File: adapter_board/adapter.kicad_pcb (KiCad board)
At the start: 2 copper layers, 100 x 80 mm, 25 parts, among them P101 CONN_01X12, P103 CONN_01X12, P104 CONN_01X02, P105 CONN_01X02, P106 CONN_01X02, P107 CONN_01X02, P108 CONN_01X01, P109 CONN_01X06, P110 CONN_01X06, P111 CONN_01X06, Q201 BC850, Q202 IRF530N, Q301 BC850, Q302 IRF530N, Q401 BC850, Q402 IRF530N

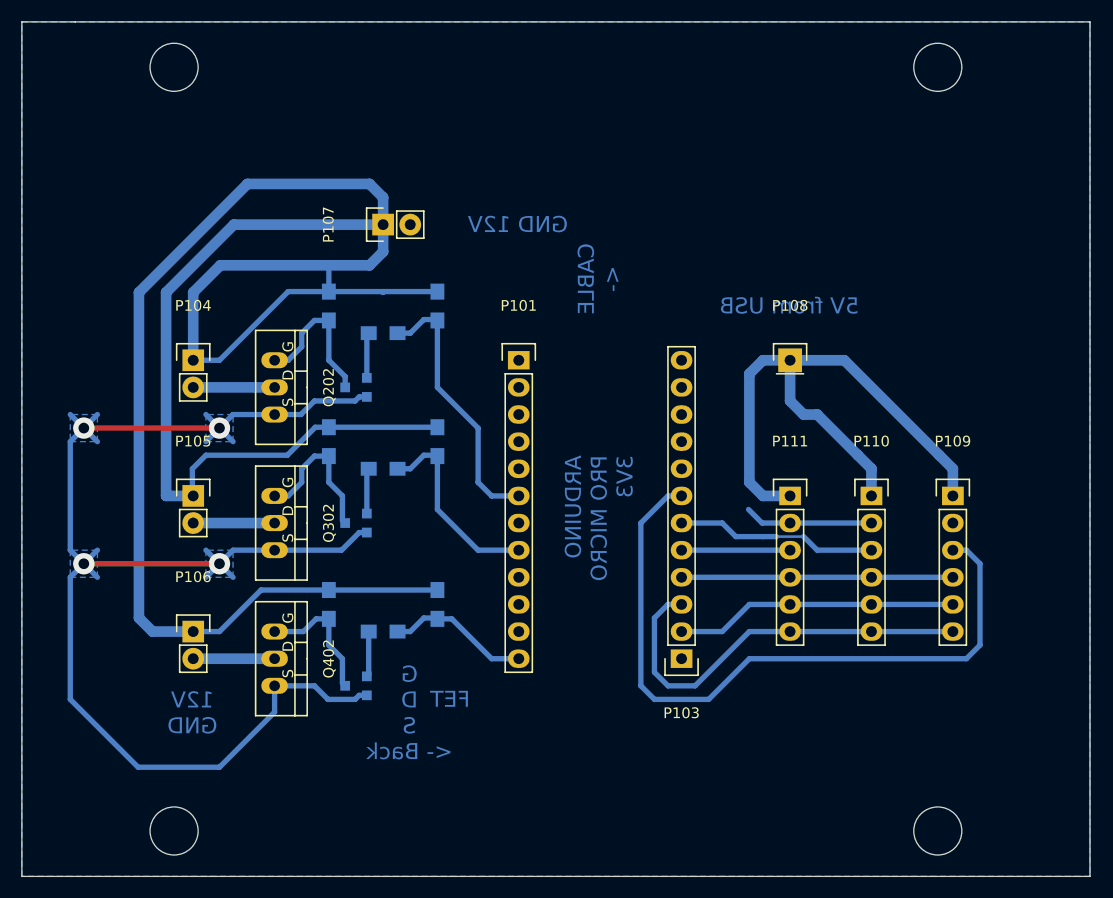
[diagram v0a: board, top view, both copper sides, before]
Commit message: enlargen pads for handsoldering
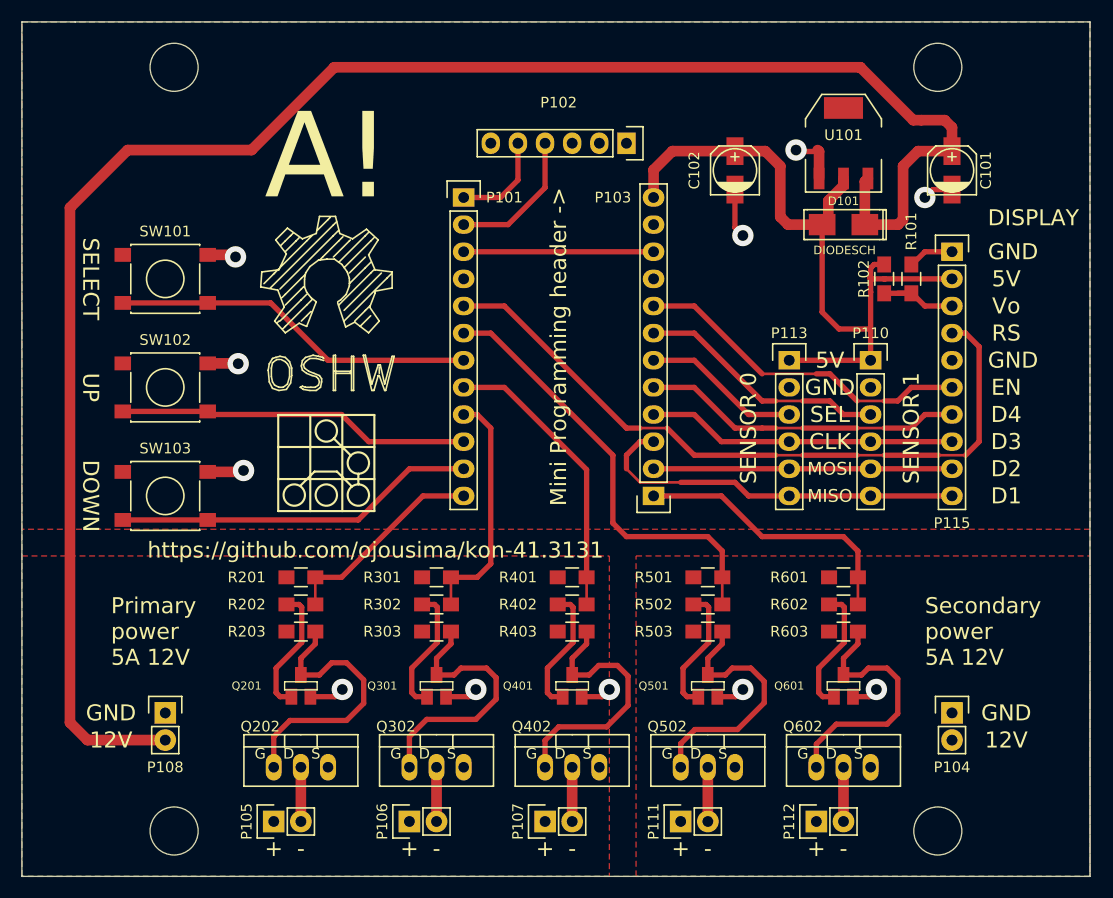
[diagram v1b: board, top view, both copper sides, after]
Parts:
- removed P109: CONN_01X06, Pin_Headers:Pin_Header_Straight_1x06
- added C101: 10u, SMD_Capacitors:c_elec_4x5.3, F.Cu at (132.1, 88.9)
- added C102: 100u, SMD_Capacitors:c_elec_4x5.3, F.Cu at (111.8, 88.9)
- added D101: DIODESCH, smd_diodes:SMA_WAVE, F.Cu at (121.9, 94.0)
- added LOGO101: OPEN_HARDWARE_2, Symbols:Symbol_OSHW-Logo_SilkScreen_BIG, F.Cu at (73.7, 80.0)
- added P102: CONN_01X06, Pin_Headers:Pin_Header_Straight_1x06, F.Cu at (101.6, 86.4)
- added P112: CONN_01X02, Pin_Headers:Pin_Header_Straight_1x02, F.Cu at (119.4, 149.9)
- added P113: CONN_01X06, Pin_Headers:Pin_Header_Straight_1x06, F.Cu at (116.8, 106.7)
- added P115: CONN_01X10, Pin_Headers:Pin_Header_Straight_1x10, F.Cu at (132.1, 96.5)
- added Q501: BC850, smd_packages_fork:SOT23EBC, F.Cu at (109.2, 137.2)
- added Q502: IRF530N, Transistors_TO-220:TO-220_FET-GDS_Vertical, F.Cu at (109.2, 144.8)
- added Q601: BC850, smd_packages_fork:SOT23EBC, F.Cu at (121.9, 137.2)
- added Q602: IRF530N, Transistors_TO-220:TO-220_FET-GDS_Vertical, F.Cu at (121.9, 144.8)
- added R101: R, Resistors_SMD:R_0805_HandSoldering, F.Cu at (125.7, 99.1)
- added R102: R, Resistors_SMD:R_0805_HandSoldering, F.Cu at (128.3, 99.1)
- added R501: 10k, Resistors_SMD:R_0805_HandSoldering, F.Cu at (109.2, 127.0)
- added R502: 1k, Resistors_SMD:R_0805_HandSoldering, F.Cu at (109.2, 129.5)
- added R503: 10k, Resistors_SMD:R_0805_HandSoldering, F.Cu at (109.2, 132.1)
- added R601: 10k, Resistors_SMD:R_0805_HandSoldering, F.Cu at (121.9, 127.0)
- added R602: 1k, Resistors_SMD:R_0805_HandSoldering, F.Cu at (121.9, 129.5)
- added R603: 10k, Resistors_SMD:R_0805_HandSoldering, F.Cu at (121.9, 132.1)
- added SW101: SPST, SMD_Switches:SW_SPST_PTS645, F.Cu at (58.4, 99.1)
- added SW102: SPST, SMD_Switches:SW_SPST_PTS645, F.Cu at (58.4, 109.2)
- added SW103: SPST, SMD_Switches:SW_SPST_PTS645, F.Cu at (58.4, 119.4)
- added U101: LD1117S50TR, SMD_Packages:SOT-223, F.Cu at (121.9, 86.4)
- P108: value CONN_01X01 -> CONN_01X02; footprint Pin_Headers:Pin_Header_Straight_1x01 -> Pin_Headers:Pin_Header_Straight_1x02
- P111: value CONN_01X06 -> CONN_01X02; footprint Pin_Headers:Pin_Header_Straight_1x06 -> Pin_Headers:Pin_Header_Straight_1x02
- Q201, Q301, Q401, R201, R202, R203, R301, R302, R303, R401, R402, R403: moved to F.Cu
- moved P104 78.3 mm to (132.1, 139.7)
- moved P108 67.2 mm to (58.4, 139.7)
- moved P107 57.9 mm to (94.0, 149.9)
- moved Q202 35.6 mm to (71.1, 144.8), turned to 0 degrees
- moved P111 32.2 mm to (106.7, 149.9), turned to 90 degrees
- moved P105 31.4 mm to (68.6, 149.9), turned to 90 degrees
- moved R203 30.6 mm to (71.1, 132.1), turned to 0 degrees
- moved Q402 29.7 mm to (96.5, 144.8), turned to 0 degrees
- moved R201 28.4 mm to (71.1, 127.0), turned to 0 degrees
- moved Q201 28.4 mm to (71.1, 137.2), turned to 180 degrees
- moved Q302 27.4 mm to (83.8, 144.8), turned to 0 degrees
- moved P106 26.9 mm to (81.3, 149.9), turned to 90 degrees
- moved R202 26.5 mm to (71.1, 129.5)
- moved R403 22.9 mm to (96.5, 132.1), turned to 0 degrees
- moved R303 20.4 mm to (83.8, 132.1), turned to 0 degrees
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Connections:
- net Net-(P103-Pad9) renamed /3V3
- P101 pad 10: Net-(P101-Pad10) -> /BT1
- P101 pad 11: Net-(P101-Pad11) -> /BT2
- P101 pad 12: /PWM2/INV_PWM -> /PWM0/INV_PWM
- P101 pad 3: Net-(P101-Pad3) -> /RESET
- P101 pad 4: /PWM0/GND -> GND
- P101 pad 5: /D2 -> /RS
- P101 pad 6: /PWM0/INV_PWM -> /PWM3/INV_PWM
- P101 pad 7: Net-(P101-Pad7) -> /BT0
- P101 pad 8: /PWM1/INV_PWM -> /PWM2/INV_PWM
- P101 pad 9: /D6 -> /PWM1/INV_PWM
- P103 pad 1: Net-(P103-Pad1) -> /PWM4/INV_PWM
- P103 pad 10: Net-(P103-Pad10) -> /RESET
- P103 pad 11: /PWM0/GND -> GND
- P103 pad 12: Net-(P103-Pad12) -> /5V
- P103 pad 5: /SEL0 -> /D4
- P103 pad 6: /SEL1 -> /SEL0
- P103 pad 7: /SEL2 -> /SEL1
- P103 pad 8: Net-(P103-Pad8) -> /SEL2
- P104 pad 1: /PWM0/12V -> GND
- P104 pad 2: /PWM0/Drain -> /PWM3/12V
- P105 pad 2: /PWM1/Drain -> /PWM0/Drain
- P106 pad 2: /PWM2/Drain -> /PWM1/Drain
- P107 pad 2: /PWM0/GND -> /PWM2/Drain
- P108 pad 1: /5V -> GND
- P110 pad 2: /PWM0/GND -> GND
- P111 pad 1: /5V -> /PWM3/12V
- P111 pad 2: /PWM0/GND -> /PWM3/Drain
- Q201 pad 1: /PWM0/GND -> GND
- Q202 pad S: /PWM0/GND -> GND
- Q301 pad 1: /PWM0/GND -> GND
- Q302 pad S: /PWM0/GND -> GND
- Q401 pad 1: /PWM0/GND -> GND
- Q402 pad S: /PWM0/GND -> GND
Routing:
- net /PWM0/GND: track 149.9 -> 0.00 mm, vias 4 -> 0
- net /RS: track 0.00 -> 66.5 mm
- net /PWM0/12V: track 218.8 -> 168.8 mm
- net /PWM3/INV_PWM: track 0.00 -> 41.4 mm
- net GND: track 0.00 -> 39.9 mm, vias 0 -> 11
- net /BT0: track 0.00 -> 34.1 mm
- net /BT2: track 0.00 -> 33.9 mm
- net /BT1: track 0.00 -> 33.5 mm
- net /SEL2: track 65.2 -> 32.1 mm
- net /D4: track 0.00 -> 30.0 mm
- net /PWM4/INV_PWM: track 0.00 -> 26.3 mm
- net Net-(Q601-Pad3): track 0.00 -> 24.6 mm
- net Net-(Q501-Pad3): track 0.00 -> 24.3 mm
- net /RESET: track 0.00 -> 17.8 mm
- net /PWM2/INV_PWM: track 13.5 -> 27.3 mm
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- added copper zone on F.Cu, net /PWM0/12V
- added copper zone on F.Cu, net /PWM3/12V
- added copper zone on B.Cu, net GND
- added copper zone on F.Cu, net GND
- removed copper zone on B.Cu, net /PWM0/GND
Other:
- net class Default: clearance 0.4 -> 0.25
- net class Power: clearance 0.4 -> 0.25
- net class thight removed
- rule trace_clearance: 0.4 -> 0.25
- board text added: "+"
- board text added: "-"
- board text added: "12V"
- board text added: "5V"
- board text added: "A!"
- board text added: "CLK"
- board text added: "D1"
- board text added: "D2"
- board text added: "D3"
- board text added: "D4"
- board text added: "DISPLAY"
- board text added: "DOWN"
- board text added: "EN"
- board text added: "GND"
- board text added: "MISO"
- board text added: "MOSI"
- board text added: "Mini Programming header ->"
- board text added: "Primary power 5A 12V"
- board text added: "RS"
- board text added: "SEL"
- board text added: "SELECT"
- board text added: "SENSOR 0"
- board text added: "SENSOR 1"
- board text added: "Secondary power 5A 12V"
- board text added: "UP"
- board text added: "Vo"
- board text added: "https://github.com/ojousima/kon-41.3131"
- board text removed: "12V GND"
- board text removed: "5V from USB"
- board text removed: "ARDUINO PRO MICRO 3V3"
- board text removed: "CABLE <-"
- board text removed: "FET"
- board text removed: "G D S <- Back"
- board text removed: "GND 12V"

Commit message: Final version
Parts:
- C102: footprint SMD_Capacitors:c_elec_4x5.3 -> SMD_Capacitors:c_elec_5x5.8
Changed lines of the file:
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@@
-(kicad_pcb (version 4) (host pcbnew "(2014-08-05 BZR 5054)-product")
+(kicad_pcb (version 4) (host pcbnew "(2015-02-06 BZR 5410)-product")
   (general
     (links 108)
     (no_connects 0)
-    (area 44.949999 74.949999 145.050001 155.050001)
+    (area 40.564287 74.899999 148.685715 165.200001)
     (thickness 1.6)
     (drawings 76)
@@
   (layers
     (0 F.Cu signal)
-    (31 B.Cu signal)
+    (31 B.Cu signal hide)
     (32 B.Adhes user)
     (33 F.Adhes user)
@@
     (visible_elements 7FFEFFFF)
     (pcbplotparams
-      (layerselection 0x00030_80000001)
-      (usegerberextensions false)
+      (layerselection 0x00008_00000000)
+      (usegerberextensions true)
       (excludeedgelayer true)
       (linewidth 0.100000)
@@
       (plotinvisibletext false)
       (padsonsilk false)
-      (subtractmaskfromsilk false)
+      (subtractmaskfromsilk true)
       (outputformat 1)
       (mirror false)
-      (drillshape 1)
+      (drillshape 0)
       (scaleselection 1)
-      (outputdirectory ""))
+      (outputdirectory gerber/))
   )
   (net 0 "")
@@
     (pad 1 smd rect (at 1.80086 0 90) (size 2.60096 1.6002) (layers F.Cu F.Paste F.Mask)
       (net 12 /PWM0/12V))
-    (pad 2 smd rect (at -1.80086 0 90) (size 2.60096 1.6002) (layers F.Cu F.Paste F.Mask)
-      (net 40 GND))
-    (model Capacitors_SMD.3dshapes/c_elec_4x5.3.wrl
-      (at (xyz 0 0 0))
-      (scale (xyz 1 1 1))
-      (rotate (xyz 0 0 0))
-    )
-  )
-  (module SMD_Capacitors:c_elec_4x5.3 (layer F.Cu)
-    (at 111.76 88.9 90)
-    (descr "SMT capacitor, aluminium electrolytic, 4x5.3")
-    (fp_text reference C102 (at 0 -3.81 90) (layer F.SilkS)
-      (effects (font (size 1 1) (thickness 0.15)))
-    )
-    (fp_text value 100u (at 0 2.794 90) (layer F.Fab)
-      (effects (font (size 1 1) (thickness 0.15)))
-    )
-    (fp_line (start 1.651 0) (end 0.889 0) (layer F.SilkS) (width 0.15))
-    (fp_line (start 1.27 -0.381) (end 1.27 0.381) (layer F.SilkS) (width 0.15))
-    (fp_line (start 1.524 2.286) (end -2.286 2.286) (layer F.SilkS) (width 0.15))
-    (fp_line (start 2.286 -1.524) (end 2.286 1.524) (layer F.SilkS) (width 0.15))
-    (fp_line (start 1.524 2.286) (end 2.286 1.524) (layer F.SilkS) (width 0.15))
-    (fp_line (start 1.524 -2.286) (end -2.286 -2.286) (layer F.SilkS) (width 0.15))
-    (fp_line (start 1.524 -2.286) (end 2.286 -1.524) (layer F.SilkS) (width 0.15))
-    (fp_line (start -2.032 0.127) (end -2.032 -0.127) (layer F.SilkS) (width 0.15))
-    (fp_line (start -1.905 -0.635) (end -1.905 0.635) (layer F.SilkS) (width 0.15))
-    (fp_line (start -1.778 0.889) (end -1.778 -0.889) (layer F.SilkS) (width 0.15))
-    (fp_line (start -1.651 1.143) (end -1.651 -1.143) (layer F.SilkS) (width 0.15))
-    (fp_line (start -1.524 -1.27) (end -1.524 1.27) (layer F.SilkS) (width 0.15))
-    (fp_line (start -1.397 1.397) (end -1.397 -1.397) (layer F.SilkS) (width 0.15))
-    (fp_line (start -1.27 -1.524) (end -1.27 1.524) (layer F.SilkS) (width 0.15))
-    (fp_line (start -1.143 -1.651) (end -1.143 1.651) (layer F.SilkS) (width 0.15))
-    (fp_circle (center 0 0) (end -2.032 0) (layer F.SilkS) (width 0.15))
-    (fp_line (start -2.286 -2.286) (end -2.286 2.286) (layer F.SilkS) (width 0.15))
-    (pad 1 smd rect (at 1.80086 0 90) (size 2.60096 1.6002) (layers F.Cu F.Paste F.Mask)
-      (net 16 /5V))
     (pad 2 smd rect (at -1.80086 0 90) (size 2.60096 1.6002) (layers F.Cu F.Paste F.Mask)
       (net 40 GND))
@@
     (fp_line (start -1.99898 23.50008) (end -1.09982 21.20138) (layer F.SilkS) (width 0.15))
   )
+  (module SMD_Capacitors:c_elec_5x5.8 (layer F.Cu)
+    (at 111.76 88.9 90)
+    (descr "SMT capacitor, aluminium electrolytic, 5x5.8")
+    (fp_text reference C102 (at 0 -3.175 90) (layer F.SilkS)
+      (effects (font (size 1 1) (thickness 0.15)))
+    )
+    (fp_text value 100u (at 0 3.175 90) (layer F.Fab)
+      (effects (font (size 1 1) (thickness 0.15)))
+    )
+    (fp_line (start -2.286 -0.635) (end -2.286 0.762) (layer F.SilkS) (width 0.15))
+    (fp_line (start -2.159 -0.889) (end -2.159 0.889) (layer F.SilkS) (width 0.15))
+    (fp_line (start -2.032 -1.27) (end -2.032 1.27) (layer F.SilkS) (width 0.15))
+    (fp_line (start -1.905 1.397) (end -1.905 -1.397) (layer F.SilkS) (width 0.15))
+    (fp_line (start -1.778 -1.524) (end -1.778 1.524) (layer F.SilkS) (width 0.15))
+    (fp_line (start -1.651 1.651) (end -1.651 -1.651) (layer F.SilkS) (width 0.15))
+    (fp_line (start -1.524 -1.778) (end -1.524 1.778) (layer F.SilkS) (width 0.15))
+    (fp_circle (center 0 0) (end -2.413 0) (layer F.SilkS) (width 0.15))
+    (fp_line (start -2.667 -2.667) (end 1.905 -2.667) (layer F.SilkS) (width 0.15))
+    (fp_line (start 1.905 -2.667) (end 2.667 -1.905) (layer F.SilkS) (width 0.15))
+    (fp_line (start 2.667 -1.905) (end 2.667 1.905) (layer F.SilkS) (width 0.15))
+    (fp_line (start 2.667 1.905) (end 1.905 2.667) (layer F.SilkS) (width 0.15))
+    (fp_line (start 1.905 2.667) (end -2.667 2.667) (layer F.SilkS) (width 0.15))
+    (fp_line (start -2.667 2.667) (end -2.667 -2.667) (layer F.SilkS) (width 0.15))
+    (fp_line (start 2.159 0) (end 1.397 0) (layer F.SilkS) (width 0.15))
+    (fp_line (start 1.778 -0.381) (end 1.778 0.381) (layer F.SilkS) (width 0.15))
+    (pad 1 smd rect (at 2.19964 0 90) (size 2.99974 1.6002) (layers F.Cu F.Paste F.Mask)
+      (net 16 /5V))
+    (pad 2 smd rect (at -2.19964 0 90) (size 2.99974 1.6002) (layers F.Cu F.Paste F.Mask)
+      (net 40 GND))
+    (model Capacitors_SMD.3dshapes/c_elec_5x5.8.wrl
+      (at (xyz 0 0 0))
+      (scale (xyz 1 1 1))
+      (rotate (xyz 0 0 0))
+    )
+  )
   (gr_text https://github.com/ojousima/kon-41.3131 (at 78.105 124.46) (layer F.SilkS)
